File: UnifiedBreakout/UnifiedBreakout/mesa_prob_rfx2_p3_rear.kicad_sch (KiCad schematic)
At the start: 1 part, among them J11 MESA P3 REAR IO

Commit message: WIP updating breakout for electrical enclosure
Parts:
- J11: symbol UnifiedBreakout-rescue:DB25_Female_MountingHoles-Connector -> Connector:DB25_Receptacle_MountingHoles; Alternative MPN L77SDB25SA4CH4F -> (none); Farnell PN (none) -> 2059751; MPN ID25S33E4GX00LF -> 5747846-4; Manufacturer Amphenol -> AMP - TE Connectivity
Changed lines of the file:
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@@
-(kicad_sch (version 20211123) (generator eeschema)
+(kicad_sch (version 20230121) (generator eeschema)
   (paper "A4")
   (junction (at 93.98 105.41) (diameter 0.9144) (color 0 0 0 0)
@@
   )
   (wire (pts (xy 93.98 80.01) (xy 93.98 74.93))
-    (stroke (width 0) (type solid) (color 0 0 0 0))
+    (stroke (width 0) (type solid))
   )
   (wire (pts (xy 90.17 90.17) (xy 90.17 127))
-    (stroke (width 0) (type solid) (color 0 0 0 0))
+    (stroke (width 0) (type solid))
   )
   (wire (pts (xy 93.98 100.33) (xy 93.98 105.41))
-    (stroke (width 0) (type solid) (color 0 0 0 0))
+    (stroke (width 0) (type solid))
   )
   (wire (pts (xy 90.17 127) (xy 135.89 127))
-    (stroke (width 0) (type solid) (color 0 0 0 0))
+    (stroke (width 0) (type solid))
   )
   (wire (pts (xy 135.89 118.11) (xy 135.89 127))
-    (stroke (width 0) (type solid) (color 0 0 0 0))
+    (stroke (width 0) (type solid))
   )
   (wire (pts (xy 93.98 95.25) (xy 93.98 100.33))
-    (stroke (width 0) (type solid) (color 0 0 0 0))
+    (stroke (width 0) (type solid))
   )
   (wire (pts (xy 93.98 74.93) (xy 128.27 74.93))
-    (stroke (width 0) (type solid) (color 0 0 0 0))
+    (stroke (width 0) (type solid))
   )
   (wire (pts (xy 93.98 80.01) (xy 128.27 80.01))
-    (stroke (width 0) (type solid) (color 0 0 0 0))
+    (stroke (width 0) (type solid))
   )
   (wire (pts (xy 135.89 127) (xy 135.89 128.27))
-    (stroke (width 0) (type solid) (color 0 0 0 0))
+    (stroke (width 0) (type solid))
   )
   (wire (pts (xy 93.98 110.49) (xy 93.98 116.84))
-    (stroke (width 0) (type solid) (color 0 0 0 0))
+    (stroke (width 0) (type solid))
   )
   (wire (pts (xy 93.98 95.25) (xy 128.27 95.25))
-    (stroke (width 0) (type solid) (color 0 0 0 0))
+    (stroke (width 0) (type solid))
   )
   (wire (pts (xy 93.98 90.17) (xy 93.98 85.09))
-    (stroke (width 0) (type solid) (color 0 0 0 0))
+    (stroke (width 0) (type solid))
   )
   (wire (pts (xy 93.98 105.41) (xy 93.98 110.49))
-    (stroke (width 0) (type solid) (color 0 0 0 0))
+    (stroke (width 0) (type solid))
   )
   (wire (pts (xy 93.98 90.17) (xy 90.17 90.17))
-    (stroke (width 0) (type solid) (color 0 0 0 0))
+    (stroke (width 0) (type solid))
   )
   (wire (pts (xy 93.98 110.49) (xy 128.27 110.49))
-    (stroke (width 0) (type solid) (color 0 0 0 0))
+    (stroke (width 0) (type solid))
   )
   (wire (pts (xy 93.98 100.33) (xy 128.27 100.33))
-    (stroke (width 0) (type solid) (color 0 0 0 0))
+    (stroke (width 0) (type solid))
   )
   (wire (pts (xy 93.98 105.41) (xy 128.27 105.41))
-    (stroke (width 0) (type solid) (color 0 0 0 0))
+    (stroke (width 0) (type solid))
   )
   (wire (pts (xy 93.98 85.09) (xy 93.98 80.01))
-    (stroke (width 0) (type solid) (color 0 0 0 0))
+    (stroke (width 0) (type solid))
   )
   (wire (pts (xy 93.98 90.17) (xy 128.27 90.17))
-    (stroke (width 0) (type solid) (color 0 0 0 0))
+    (stroke (width 0) (type solid))
   )
   (wire (pts (xy 93.98 85.09) (xy 128.27 85.09))
-    (stroke (width 0) (type solid) (color 0 0 0 0))
+    (stroke (width 0) (type solid))
   )
-  (hierarchical_label "IO_07" (shape bidirectional) (at 128.27 69.85 180)
+  (hierarchical_label "IO_07" (shape bidirectional) (at 128.27 69.85 180) (fields_autoplaced)
     (effects (font (size 1.27 1.27)) (justify right))
   )
-  (hierarchical_label "IO_16_QUAD_00_IDX" (shape input) (at 128.27 113.03 180)
+  (hierarchical_label "IO_16_QUAD_00_IDX" (shape input) (at 128.27 113.03 180) (fields_autoplaced)
     (effects (font (size 1.27 1.27)) (justify right))
   )
-  (hierarchical_label "IO_15_QUAD_00_B" (shape input) (at 128.27 107.95 180)
+  (hierarchical_label "IO_15_QUAD_00_B" (shape input) (at 128.27 107.95 180) (fields_autoplaced)
     (effects (font (size 1.27 1.27)) (justify right))
   )
-  (hierarchical_label "IO_02_STEPGEN_00_STEP" (shape output) (at 128.27 57.15 180)
+  (hierarchical_label "IO_02_STEPGEN_00_STEP" (shape output) (at 128.27 57.15 180) (fields_autoplaced)
     (effects (font (size 1.27 1.27)) (justify right))
   )
-  (hierarchical_label "IO_03" (shape bidirectional) (at 128.27 59.69 180)
+  (hierarchical_label "IO_03" (shape bidirectional) (at 128.27 59.69 180) (fields_autoplaced)
     (effects (font (size 1.27 1.27)) (justify right))
   )
-  (hierarchical_label "IO_12_STEPGEN_03_DIR" (shape output) (at 128.27 92.71 180)
+  (hierarchical_label "IO_12_STEPGEN_03_DIR" (shape output) (at 128.27 92.71 180) (fields_autoplaced)
     (effects (font (size 1.27 1.27)) (justify right))
   )
-  (hierarchical_label "IO_10_STEPGEN_02_DIR" (shape output) (at 128.27 82.55 180)
+  (hierarchical_label "IO_10_STEPGEN_02_DIR" (shape output) (at 128.27 82.55 180) (fields_autoplaced)
     (effects (font (size 1.27 1.27)) (justify right))
   )
-  (hierarchical_label "IO_05_PWMGEN_00_DIR" (shape output) (at 128.27 64.77 180)
+  (hierarchical_label "IO_05_PWMGEN_00_DIR" (shape output) (at 128.27 64.77 180) (fields_autoplaced)
     (effects (font (size 1.27 1.27)) (justify right))
   )
-  (hierarchical_label "IO_13" (shape bidirectional) (at 128.27 97.79 180)
+  (hierarchical_label "IO_13" (shape bidirectional) (at 128.27 97.79 180) (fields_autoplaced)
     (effects (font (size 1.27 1.27)) (justify right))
   )
-  (hierarchical_label "IO_09_STEPGEN_02_STEP" (shape output) (at 128.27 77.47 180)
+  (hierarchical_label "IO_09_STEPGEN_02_STEP" (shape output) (at 128.27 77.47 180) (fields_autoplaced)
     (effects (font (size 1.27 1.27)) (justify right))
   )
-  (hierarchical_label "MESA_5V" (shape output) (at 93.98 116.84 270)
+  (hierarchical_label "MESA_5V" (shape output) (at 93.98 116.84 270) (fields_autoplaced)
     (effects (font (size 1.27 1.27)) (justify right))
   )
-  (hierarchical_label "IO_00" (shape bidirectional) (at 128.27 52.07 180)
+  (hierarchical_label "IO_00" (shape bidirectional) (at 128.27 52.07 180) (fields_autoplaced)
     (effects (font (size 1.27 1.27)) (justify right))
   )
-  (hierarchical_label "IO_01_PWMGEN_00_PWM" (shape output) (at 128.27 54.61 180)
+  (hierarchical_label "IO_01_PWMGEN_00_PWM" (shape output) (at 128.27 54.61 180) (fields_autoplaced)
     (effects (font (size 1.27 1.27)) (justify right))
   )
-  (hierarchical_label "IO_08_STEPGEN_01_DIR" (shape output) (at 128.27 72.39 180)
+  (hierarchical_label "IO_08_STEPGEN_01_DIR" (shape output) (at 128.27 72.39 180) (fields_autoplaced)
     (effects (font (size 1.27 1.27)) (justify right))
   )
-  (hierarchical_label "IO_14_QUAD_00_A" (shape input) (at 128.27 102.87 180)
+  (hierarchical_label "IO_14_QUAD_00_A" (shape input) (at 128.27 102.87 180) (fields_autoplaced)
     (effects (font (size 1.27 1.27)) (justify right))
   )
-  (hierarchical_label "IO_11_STEPGEN_03_STEP" (shape output) (at 128.27 87.63 180)
+  (hierarchical_label "IO_11_STEPGEN_03_STEP" (shape output) (at 128.27 87.63 180) (fields_autoplaced)
     (effects (font (size 1.27 1.27)) (justify right))
   )
-  (hierarchical_label "GND" (shape output) (at 135.89 128.27 270)
+  (hierarchical_label "GND" (shape output) (at 135.89 128.27 270) (fields_autoplaced)
     (effects (font (size 1.27 1.27)) (justify right))
   )
-  (hierarchical_label "IO_04_STEPGEN_00_DIR" (shape output) (at 128.27 62.23 180)
+  (hierarchical_label "IO_04_STEPGEN_00_DIR" (shape output) (at 128.27 62.23 180) (fields_autoplaced)
     (effects (font (size 1.27 1.27)) (justify right))
   )
-  (hierarchical_label "IO_06_STEPGEN_01_STEP" (shape output) (at 128.27 67.31 180)
+  (hierarchical_label "IO_06_STEPGEN_01_STEP" (shape output) (at 128.27 67.31 180) (fields_autoplaced)
     (effects (font (size 1.27 1.27)) (justify right))
   )
-  (symbol (lib_id "UnifiedBreakout-rescue:DB25_Female_MountingHoles-Connector") (at 135.89 82.55 0) (unit 1)
-    (in_bom yes) (on_board yes)
-    (property "Reference" "J11" (id 0) (at 140.462 82.4992 0)
+  (symbol (lib_id "Connector:DB25_Receptacle_MountingHoles") (at 135.89 82.55 0) (unit 1)
+    (in_bom yes) (on_board yes) (dnp no)
+    (property "Reference" "J11" (at 140.462 82.4992 0)
       (effects (font (size 1.27 1.27)) (justify left))
     )
-    (property "Value" "MESA P3 REAR IO" (id 1) (at 140.462 84.8106 0)
+    (property "Value" "MESA P3 REAR IO" (at 140.462 84.8106 0)
       (effects (font (size 1.27 1.27)) (justify left))
     )
-    (property "Footprint" "Connector_Dsub:DSUB-25_Female_Horizontal_P2.77x2.84mm_EdgePinOffset7.70mm_Housed_MountingHolesOffset9.12mm" (id 2) (at 135.89 82.55 0)
+    (property "Footprint" "Connector_Dsub:DSUB-25_Female_Horizontal_P2.77x2.84mm_EdgePinOffset7.70mm_Housed_MountingHolesOffset9.12mm" (at 135.89 82.55 0)
       (effects (font (size 1.27 1.27)) hide)
     )
-    (property "Datasheet" " ~" (id 3) (at 135.89 82.55 0)
+    (property "Datasheet" " ~" (at 135.89 82.55 0)
       (effects (font (size 1.27 1.27)) hide)
     )
-    (property "Alternative MPN" "L77SDB25SA4CH4F " (id 4) (at 135.89 82.55 0)
+    (property "Alternative MPN" "" (at 135.89 82.55 0)
       (effects (font (size 1.27 1.27)) hide)
     )
-    (property "MPN" "ID25S33E4GX00LF" (id 5) (at 135.89 82.55 0)
+    (property "MPN" "5747846-4 " (at 135.89 82.55 0)
       (effects (font (size 1.27 1.27)) hide)
     )
-    (property "Manufacturer" "Amphenol" (id 6) (at 135.89 82.55 0)
+    (property "Manufacturer" "AMP - TE Connectivity" (at 135.89 82.55 0)
+      (effects (font (size 1.27 1.27)) hide)
+    )
+    (property "Farnell PN" "2059751" (at 135.89 82.55 0)
       (effects (font (size 1.27 1.27)) hide)
     )
@@
     (pin "8")
     (pin "9")
+    (instances
+      (project "UnifiedBreakout"
+        (path "/e63e39d7-6ac0-4ffd-8aa3-1841a4541b55/00000000-0000-0000-0000-00005e961c58"
+          (reference "J11") (unit 1)
+        )
+      )
+    )
   )
 )

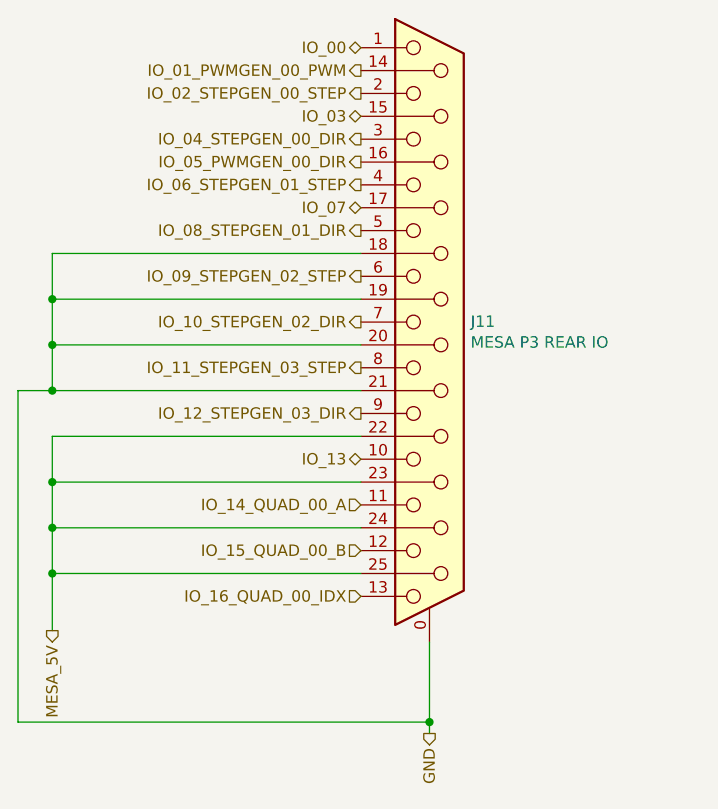
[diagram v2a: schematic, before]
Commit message: Add dual level DB25
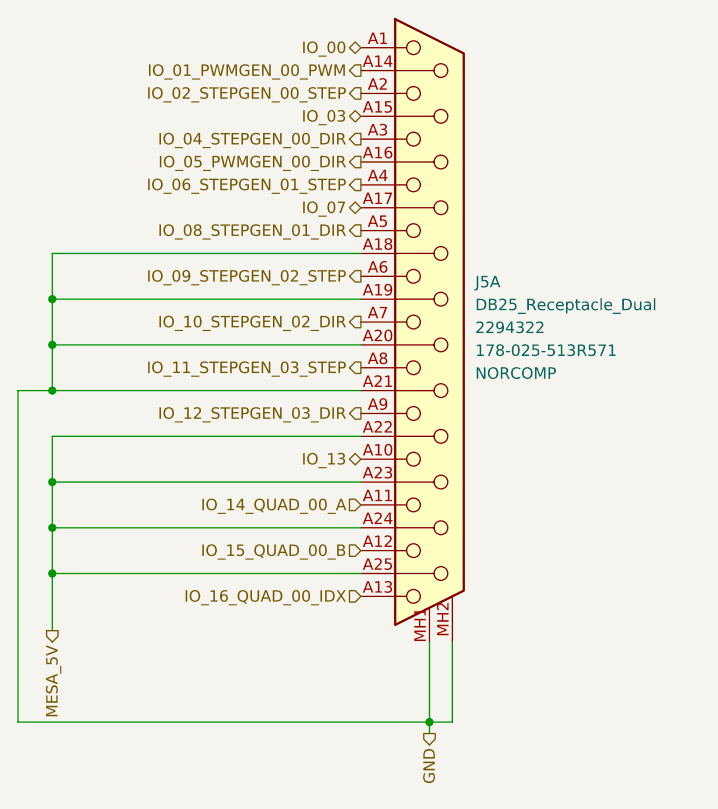
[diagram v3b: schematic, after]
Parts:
- removed J11: MESA P3 REAR IO, Connector_Dsub:DSUB-25_Female_Horizontal_P2.77x2.84mm_EdgePinOffset7.70mm_Housed_MountingHolesOffset9.12mm, symbol Connector:DB25_Receptacle_MountingHoles
- added J5: DB25_Receptacle_Dual, UnifiedBreakout:NorComp-Dual-DB25, symbol UnifiedBreakout:DB25_Receptacle_Dual
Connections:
- net GND: now also J5.A18, J5.A19, J5.A20, J5.A21, J5.MH1, J5.MH2
- net IO_00: now also J5.A1
- net IO_01_PWMGEN_00_PWM: now also J5.A14
- net IO_02_STEPGEN_00_STEP: now also J5.A2
- net IO_03: now also J5.A15
- net IO_04_STEPGEN_00_DIR: now also J5.A3
- net IO_05_PWMGEN_00_DIR: now also J5.A16
- net IO_06_STEPGEN_01_STEP: now also J5.A4
- net IO_07: now also J5.A17
- net IO_08_STEPGEN_01_DIR: now also J5.A5
- net IO_09_STEPGEN_02_STEP: now also J5.A6
- net IO_10_STEPGEN_02_DIR: now also J5.A7
- net IO_11_STEPGEN_03_STEP: now also J5.A8
- net IO_12_STEPGEN_03_DIR: now also J5.A9
- net IO_13: now also J5.A10
- net IO_14_QUAD_00_A: now also J5.A11
- net IO_15_QUAD_00_B: now also J5.A12
- net IO_16_QUAD_00_IDX: now also J5.A13
- net MESA_5V: now also J5.A22, J5.A23, J5.A24, J5.A25
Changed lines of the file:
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@@
     (stroke (width 0) (type solid))
+  )
+  (wire (pts (xy 138.43 127) (xy 135.89 127))
+    (stroke (width 0) (type default))
   )
   (wire (pts (xy 93.98 100.33) (xy 93.98 105.41))
@@
     (stroke (width 0) (type solid))
   )
+  (wire (pts (xy 138.43 118.11) (xy 138.43 127))
+    (stroke (width 0) (type default))
+  )
   (wire (pts (xy 93.98 74.93) (xy 128.27 74.93))
     (stroke (width 0) (type solid))
@@
     (effects (font (size 1.27 1.27)) (justify right))
   )
-  (symbol (lib_id "Connector:DB25_Receptacle_MountingHoles") (at 135.89 82.55 0) (unit 1)
-    (in_bom yes) (on_board yes) (dnp no)
-    (property "Reference" "J11" (at 140.462 82.4992 0)
-      (effects (font (size 1.27 1.27)) (justify left))
-    )
-    (property "Value" "MESA P3 REAR IO" (at 140.462 84.8106 0)
-      (effects (font (size 1.27 1.27)) (justify left))
-    )
-    (property "Footprint" "Connector_Dsub:DSUB-25_Female_Horizontal_P2.77x2.84mm_EdgePinOffset7.70mm_Housed_MountingHolesOffset9.12mm" (at 135.89 82.55 0)
+  (symbol (lib_id "UnifiedBreakout:DB25_Receptacle_Dual") (at 135.89 82.55 0) (unit 1)
+    (in_bom yes) (on_board yes) (dnp no) (fields_autoplaced)
+    (property "Reference" "J5" (at 140.97 78.105 0)
+      (effects (font (size 1.27 1.27)) (justify left))
+    )
+    (property "Value" "DB25_Receptacle_Dual" (at 140.97 80.645 0)
+      (effects (font (size 1.27 1.27)) (justify left))
+    )
+    (property "Footprint" "UnifiedBreakout:NorComp-Dual-DB25" (at 135.89 82.55 0)
       (effects (font (size 1.27 1.27)) hide)
     )
@@
       (effects (font (size 1.27 1.27)) hide)
     )
-    (property "Alternative MPN" "" (at 135.89 82.55 0)
-      (effects (font (size 1.27 1.27)) hide)
-    )
-    (property "MPN" "5747846-4 " (at 135.89 82.55 0)
-      (effects (font (size 1.27 1.27)) hide)
-    )
-    (property "Manufacturer" "AMP - TE Connectivity" (at 135.89 82.55 0)
-      (effects (font (size 1.27 1.27)) hide)
-    )
-    (property "Farnell PN" "2059751" (at 135.89 82.55 0)
-      (effects (font (size 1.27 1.27)) hide)
-    )
-    (pin "0")
-    (pin "1")
-    (pin "10")
-    (pin "11")
-    (pin "12")
-    (pin "13")
-    (pin "14")
-    (pin "15")
-    (pin "16")
-    (pin "17")
-    (pin "18")
-    (pin "19")
-    (pin "2")
-    (pin "20")
-    (pin "21")
-    (pin "22")
-    (pin "23")
-    (pin "24")
-    (pin "25")
-    (pin "3")
-    (pin "4")
-    (pin "5")
-    (pin "6")
-    (pin "7")
-    (pin "8")
-    (pin "9")
+    (property "Farnell PN" "2294322" (at 140.97 83.185 0)
+      (effects (font (size 1.27 1.27)) (justify left))
+    )
+    (property "MPN" "178-025-513R571" (at 140.97 85.725 0)
+      (effects (font (size 1.27 1.27)) (justify left))
+    )
+    (property "Manufacturer" "NORCOMP" (at 140.97 88.265 0)
+      (effects (font (size 1.27 1.27)) (justify left))
+    )
+    (pin "A1")
+    (pin "A10")
+    (pin "A11")
+    (pin "A12")
+    (pin "A13")
+    (pin "A14")
+    (pin "A15")
+    (pin "A16")
+    (pin "A17")
+    (pin "A18")
+    (pin "A19")
+    (pin "A2")
+    (pin "A20")
+    (pin "A21")
+    (pin "A22")
+    (pin "A23")
+    (pin "A24")
+    (pin "A25")
+    (pin "A3")
+    (pin "A4")
+    (pin "A5")
+    (pin "A6")
+    (pin "A7")
+    (pin "A8")
+    (pin "A9")
+    (pin "MH1")
+    (pin "MH2")
+    (pin "B1")
+    (pin "B10")
+    (pin "B11")
+    (pin "B12")
+    (pin "B13")
+    (pin "B14")
+    (pin "B15")
+    (pin "B16")
+    (pin "B17")
+    (pin "B18")
+    (pin "B19")
+    (pin "B2")
+    (pin "B20")
+    (pin "B21")
+    (pin "B22")
+    (pin "B23")
+    (pin "B24")
+    (pin "B25")
+    (pin "B3")
+    (pin "B4")
+    (pin "B5")
+    (pin "B6")
+    (pin "B7")
+    (pin "B8")
+    (pin "B9")
+    (pin "MH3")
+    (pin "MH4")
     (instances
       (project "UnifiedBreakout"
         (path "/e63e39d7-6ac0-4ffd-8aa3-1841a4541b55/00000000-0000-0000-0000-00005e961c58"
-          (reference "J11") (unit 1)
+          (reference "J5") (unit 1)
         )
       )

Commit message: Update IO and opto
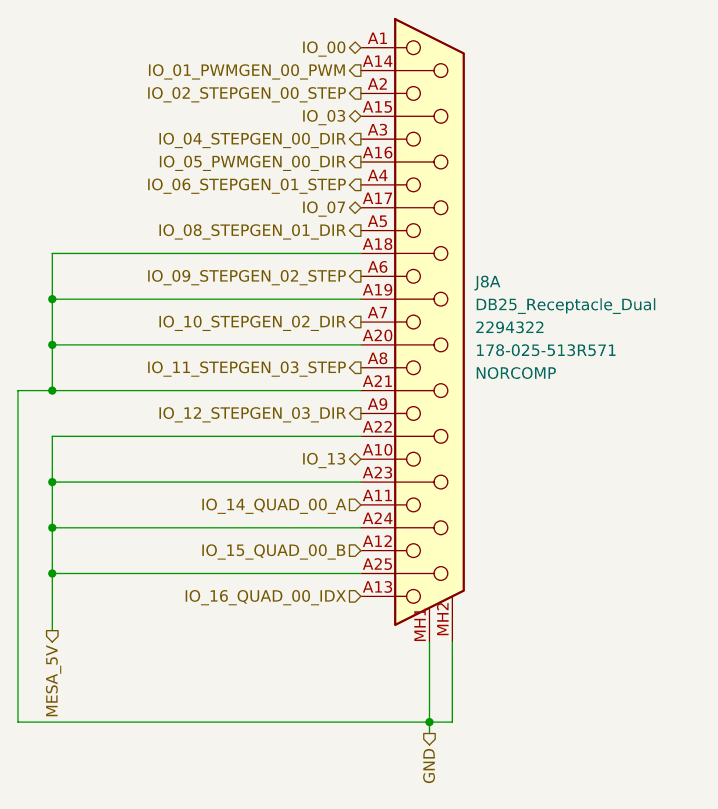
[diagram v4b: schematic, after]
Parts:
- renumbered J5 to J8
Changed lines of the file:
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@@
   (symbol (lib_id "UnifiedBreakout:DB25_Receptacle_Dual") (at 135.89 82.55 0) (unit 1)
     (in_bom yes) (on_board yes) (dnp no) (fields_autoplaced)
-    (property "Reference" "J5" (at 140.97 78.105 0)
+    (property "Reference" "J8" (at 140.97 78.105 0)
       (effects (font (size 1.27 1.27)) (justify left))
     )
@@
       (project "UnifiedBreakout"
         (path "/e63e39d7-6ac0-4ffd-8aa3-1841a4541b55/00000000-0000-0000-0000-00005e961c58"
-          (reference "J5") (unit 1)
+          (reference "J8") (unit 1)
         )
       )

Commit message: Some layout
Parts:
- renumbered J8 to J10
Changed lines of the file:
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@@
   (symbol (lib_id "UnifiedBreakout:DB25_Receptacle_Dual") (at 135.89 82.55 0) (unit 1)
     (in_bom yes) (on_board yes) (dnp no) (fields_autoplaced)
-    (property "Reference" "J8" (at 140.97 78.105 0)
+    (property "Reference" "J10" (at 140.97 78.105 0)
       (effects (font (size 1.27 1.27)) (justify left))
     )
@@
       (project "UnifiedBreakout"
         (path "/e63e39d7-6ac0-4ffd-8aa3-1841a4541b55/00000000-0000-0000-0000-00005e961c58"
-          (reference "J8") (unit 1)
+          (reference "J10") (unit 1)
         )
       )
